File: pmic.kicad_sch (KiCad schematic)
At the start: 13 parts, among them J3 Battery Connector, SW2 PWR_BTN, U1 NPM1300-CAAA-R

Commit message: added peripherals pins
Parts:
- added C30, C31: 1u, symbol Device:C
- added C32, C33: 2.2u, symbol Device:C
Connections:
- net GND: now also C30.1, C31.1, C32.1, C33.1; no longer U1.B4 (LSIN1/VINLDO1), U1.B5 (LSIN2/VINLDO2)
- net VSYS: now also U1.B4 (LSIN1/VINLDO1), U1.B5 (LSIN2/VINLDO2), C30.2, C31.2
- net LSOUT1: now reaches U1.A4 (LSOUT1/VOUTLDO1)
- net LSOUT1: now also C33.2
- net LSOUT2: now reaches U1.A5 (LSOUT2/VOUTLDO2)
- net LSOUT2: now also C32.2
- no-connect marks 6 -> 4
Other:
- moved on the sheet: C22, D1

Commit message: assigned footprint and created PCB file
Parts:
- C20, C21: footprint (none) -> Capacitor_SMD:C_0805_2012Metric
- C22, C30, C31, C32, C33: footprint (none) -> Capacitor_SMD:C_0603_1608Metric
- D1: footprint (none) -> LED_SMD:LED_RGB_1210
- J3: footprint (none) -> Connector_PinHeader_2.54mm:PinHeader_1x02_P2.54mm_Vertical
- L1, L2: footprint (none) -> Inductor_SMD:L_0805_2012Metric
- R2, R3, R4, TH1: footprint (none) -> Resistor_SMD:R_0603_1608Metric
- SW2: footprint (none) -> Button_Switch_SMD:SW_Push_1P1T_NO_CK_KMR2
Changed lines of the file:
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@@
 			)
 		)
-		(property "Footprint" ""
+		(property "Footprint" "Capacitor_SMD:C_0603_1608Metric"
 			(at 116.5352 86.36 0)
 			(hide yes)
@@
 			)
 		)
-		(property "Footprint" ""
+		(property "Footprint" "Capacitor_SMD:C_0603_1608Metric"
 			(at 208.5848 86.36 0)
 			(hide yes)
@@
 			)
 		)
-		(property "Footprint" ""
+		(property "Footprint" "Button_Switch_SMD:SW_Push_1P1T_NO_CK_KMR2"
 			(at 204.47 124.46 0)
 			(hide yes)
@@
 			)
 		)
-		(property "Footprint" ""
+		(property "Footprint" "Resistor_SMD:R_0603_1608Metric"
 			(at 115.57 102.87 0)
 			(hide yes)
@@
 			)
 		)
-		(property "Footprint" ""
+		(property "Footprint" "Capacitor_SMD:C_0603_1608Metric"
 			(at 102.5652 86.36 0)
 			(hide yes)
@@
 			)
 		)
-		(property "Footprint" ""
+		(property "Footprint" "Resistor_SMD:R_0603_1608Metric"
 			(at 120.65 132.588 90)
 			(hide yes)
@@
 			)
 		)
-		(property "Footprint" ""
+		(property "Footprint" "Connector_PinHeader_2.54mm:PinHeader_1x02_P2.54mm_Vertical"
 			(at 71.12 57.15 0)
 			(hide yes)
@@
 			)
 		)
-		(property "Footprint" ""
+		(property "Footprint" "Inductor_SMD:L_0805_2012Metric"
 			(at 191.77 110.49 0)
 			(hide yes)
@@
 			)
 		)
-		(property "Footprint" ""
+		(property "Footprint" "Capacitor_SMD:C_0603_1608Metric"
 			(at 214.63 77.7748 0)
 			(hide yes)
@@
 			)
 		)
-		(property "Footprint" ""
+		(property "Footprint" "Resistor_SMD:R_0603_1608Metric"
 			(at 99.568 114.3 90)
 			(hide yes)
@@
 			)
 		)
-		(property "Footprint" ""
+		(property "Footprint" "LED_SMD:LED_RGB_1210"
 			(at 226.06 99.06 0)
 			(hide yes)
@@
 			)
 		)
-		(property "Footprint" ""
+		(property "Footprint" "Inductor_SMD:L_0805_2012Metric"
 			(at 193.04 120.65 0)
 			(hide yes)
@@
 			)
 		)
-		(property "Footprint" ""
+		(property "Footprint" "Capacitor_SMD:C_0603_1608Metric"
 			(at 197.1548 86.36 0)
 			(hide yes)
@@
 			)
 		)
-		(property "Footprint" ""
+		(property "Footprint" "Resistor_SMD:R_0603_1608Metric"
 			(at 110.998 115.57 90)
 			(hide yes)
@@
 			)
 		)
-		(property "Footprint" ""
+		(property "Footprint" "Capacitor_SMD:C_0805_2012Metric"
 			(at 180.34 57.4548 0)
 			(hide yes)
@@
 			)
 		)
-		(property "Footprint" ""
+		(property "Footprint" "Capacitor_SMD:C_0805_2012Metric"
 			(at 196.5452 74.93 0)
 			(hide yes)

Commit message: migrated display power with lora
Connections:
- net +3.3V_DISP renamed +3.3V_DP_LORA
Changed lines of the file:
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@@
 			)
 		)
-		(property "Value" "+3.3V_DISP"
+		(property "Value" "+3.3V_DP_LORA"
 			(at 201.93 109.2199 90)
 			(show_name no)

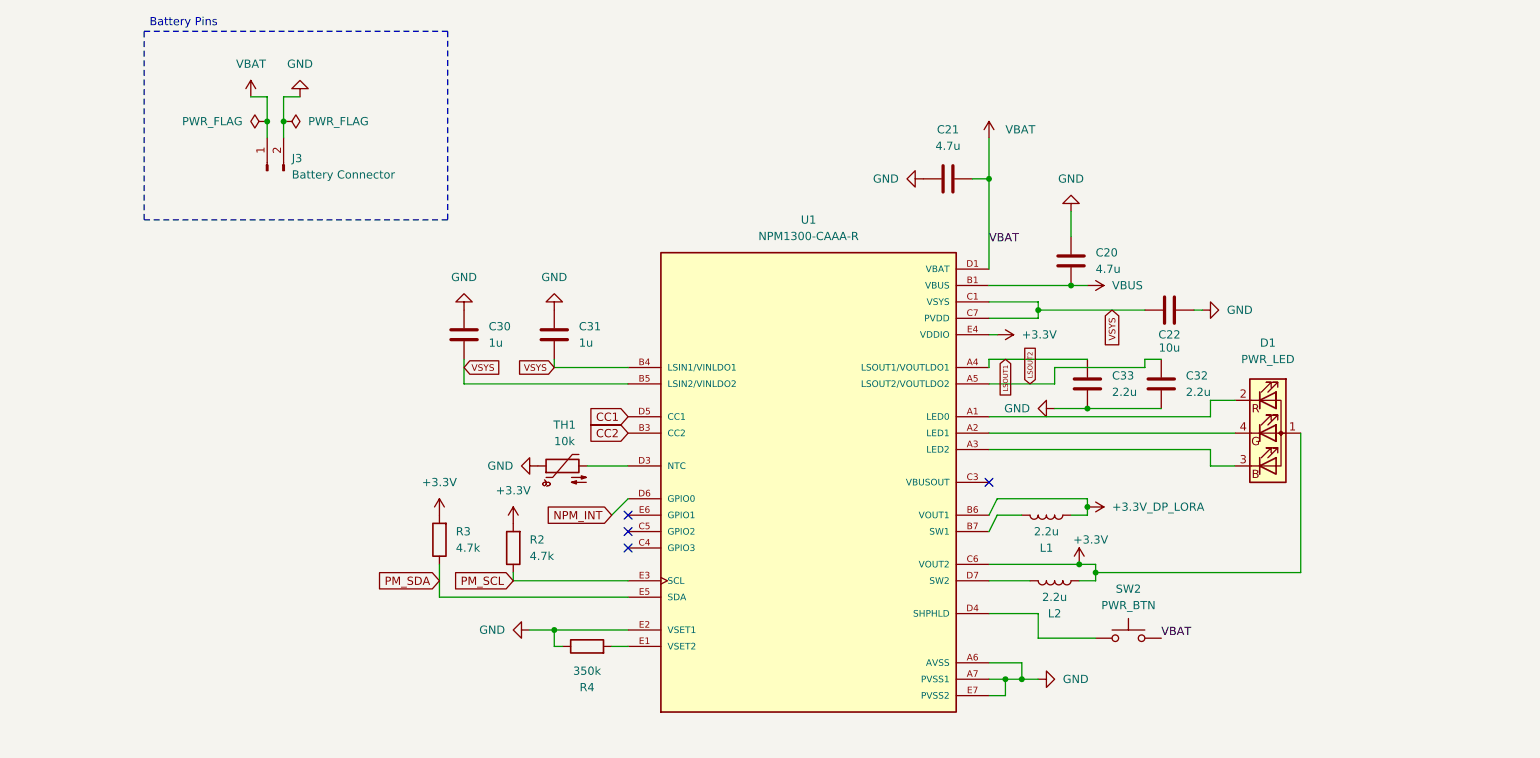
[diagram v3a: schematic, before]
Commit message: changed NPM1300 BGA to QFN package
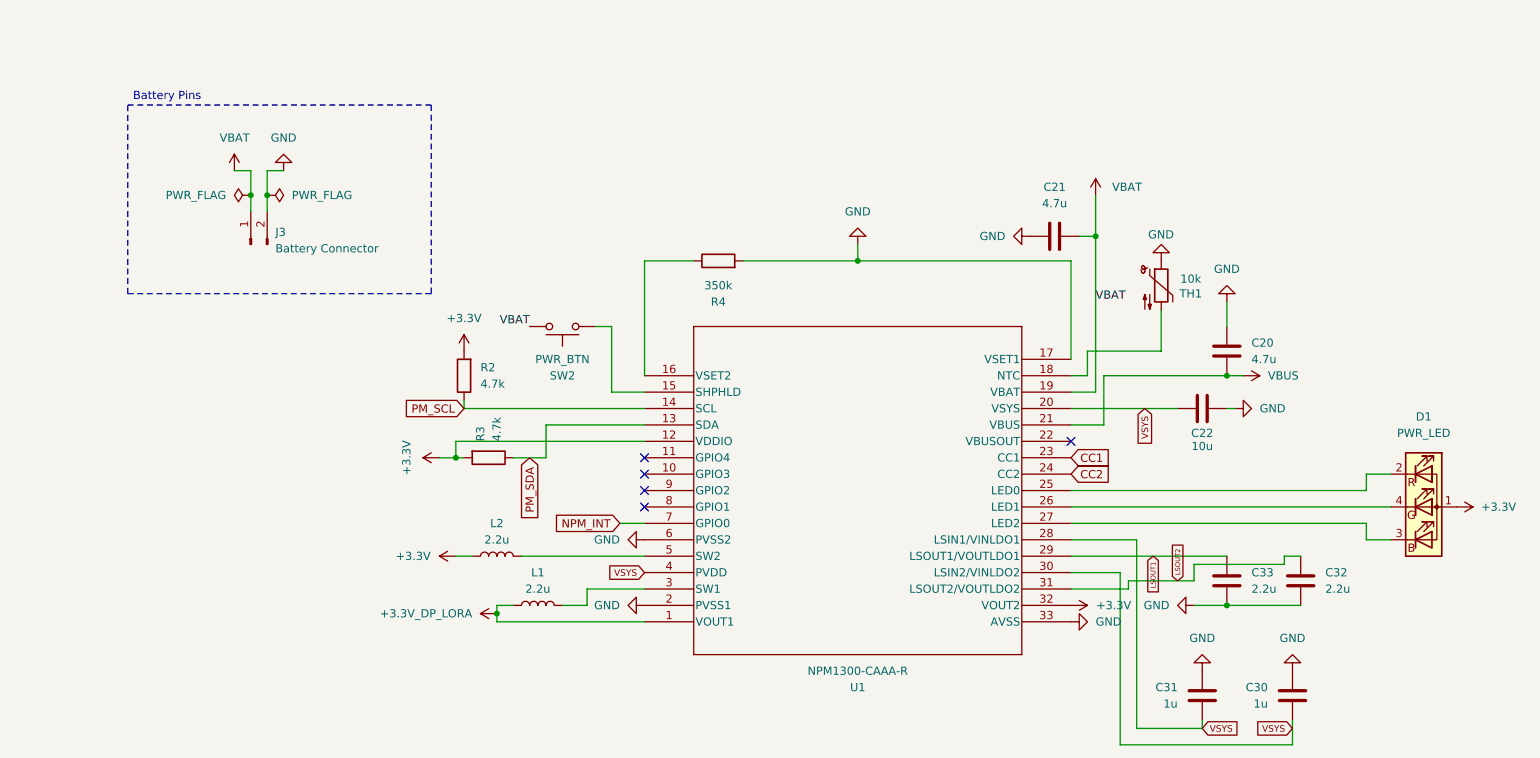
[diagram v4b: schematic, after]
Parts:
- U1: footprint TheSummitProject:BGA35N44X41P5X7_237X307X51 -> TheSummitProject:QFN32_5X5_NOR; symbol TheSummitProject:NPM1300-CAAA-R -> TheSummitProject:NPM1300-QEAA-R7
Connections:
- net +3.3V: now also U1.12 (VDDIO), U1.32 (VOUT2); no longer U1.C6 (VOUT2), U1.E4 (VDDIO)
- net +3.3V_DP_LORA: now also U1.1 (VOUT1); no longer U1.B6 (VOUT1)
- net CC1: now also U1.23 (CC1); no longer U1.D5 (CC1)
- net CC2: now also U1.24 (CC2); no longer U1.B3 (CC2)
- net GND: now also R4.2, U1.17 (VSET1), U1.2 (PVSS1), U1.33 (AVSS), U1.6 (PVSS2); no longer R4.1, U1.A6 (AVSS), U1.A7 (PVSS1), U1.E2 (VSET1), U1.E7 (PVSS2)
- net LSOUT1: now also U1.29 (LSOUT1/VOUTLDO1); no longer U1.A4 (LSOUT1/VOUTLDO1)
- net LSOUT2: now also U1.31 (LSOUT2/VOUTLDO2); no longer U1.A5 (LSOUT2/VOUTLDO2)
- net NPM_INT: now also U1.7 (GPIO0); no longer U1.D6 (GPIO0)
- net PM_SCL: now also U1.14 (SCL); no longer U1.E3 (SCL)
- net PM_SDA: now also U1.13 (SDA); no longer U1.E5 (SDA)
- net VBAT: now also U1.19 (VBAT); no longer U1.D1 (VBAT), U1.D2 (VBAT)
- net VBUS: now also U1.21 (VBUS); no longer U1.B1 (VBUS), U1.B2 (VBUS)
- net VSYS: now also U1.20 (VSYS), U1.28 (LSIN1/VINLDO1), U1.30 (LSIN2/VINLDO2), U1.4 (PVDD); no longer U1.B4 (LSIN1/VINLDO1), U1.B5 (LSIN2/VINLDO2), U1.C1 (VSYS), U1.C2 (VSYS), U1.C7 (PVDD)
- net at SW2.1: now also U1.15 (SHPHLD); no longer U1.D4 (SHPHLD)
- net at TH1.2: now also U1.18 (NTC); no longer U1.D3 (NTC)
- net at D1.2 (RK): now also U1.25 (LED0); no longer U1.A1 (LED0)
- net at D1.4 (GK): now also U1.26 (LED1); no longer U1.A2 (LED1)
- net at D1.3 (BK): now also U1.27 (LED2); no longer U1.A3 (LED2)
- net at L1.1: now also U1.3 (SW1); no longer U1.B7 (SW1)
- net at L2.1: now also U1.5 (SW2); no longer U1.D7 (SW2)
- new net: R4.1, U1.16 (VSET2)
- no-connect marks 4 -> 5
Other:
- moved on the sheet: C20, C21, C22, D1, J3, L1

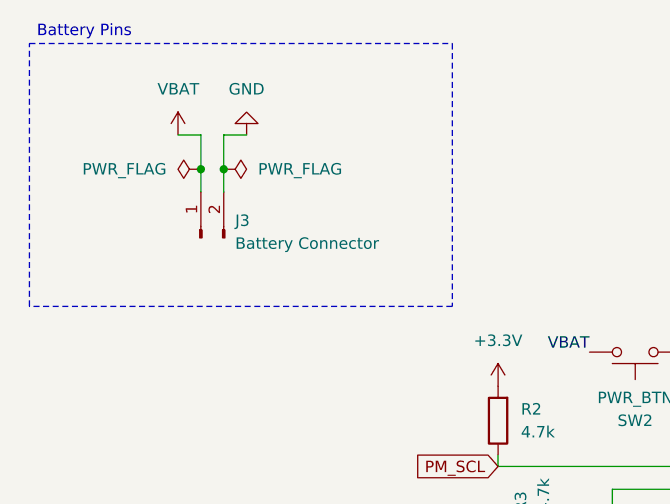
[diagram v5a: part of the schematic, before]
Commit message: Changed pcb to 4 layers and completed 50% traces
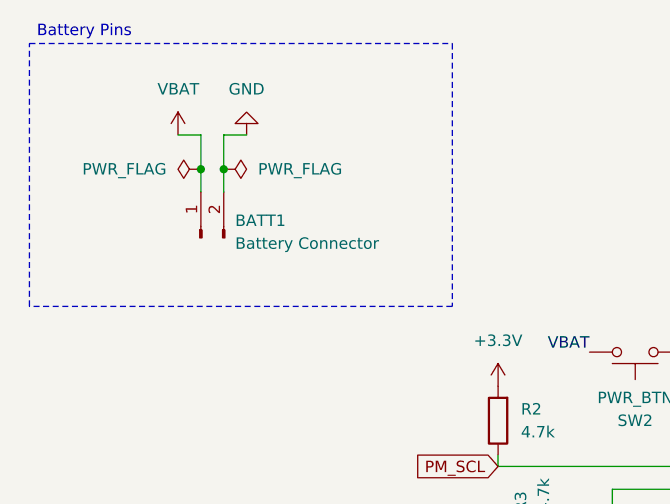
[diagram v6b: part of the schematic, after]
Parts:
- renumbered J3 to BATT1
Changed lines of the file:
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@@
 		(dnp no)
 		(fields_autoplaced yes)
-		(property "Reference" "J3"
+		(property "Reference" "BATT1"
 			(at 72.39 66.6749 90)
 			(show_name no)
@@
 			(project "TheSummitProject"
 				(path "/589d7319-43ab-496c-8236-77eb6db23a7f"
-					(reference "J3")
+					(reference "BATT1")
 					(unit 1)
 				)

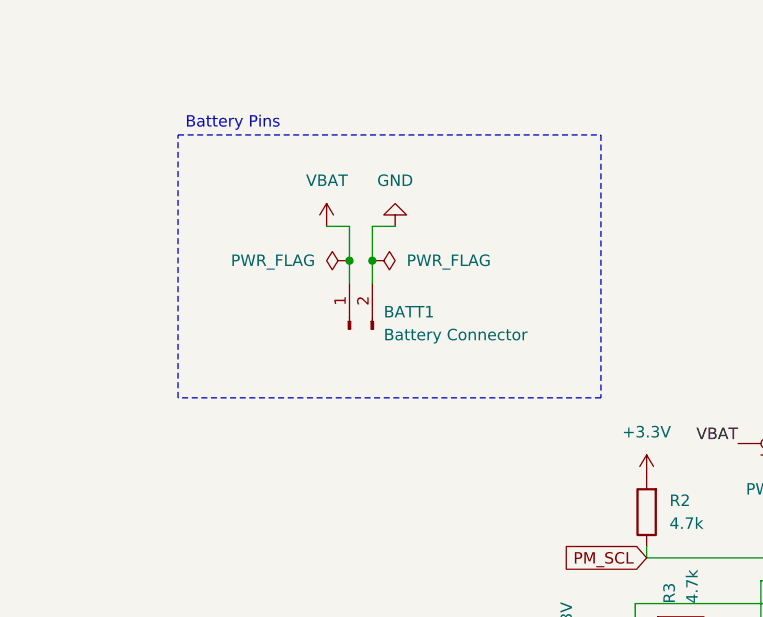
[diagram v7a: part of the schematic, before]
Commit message: Added reverse polarity protection circuit, PCB not implemented
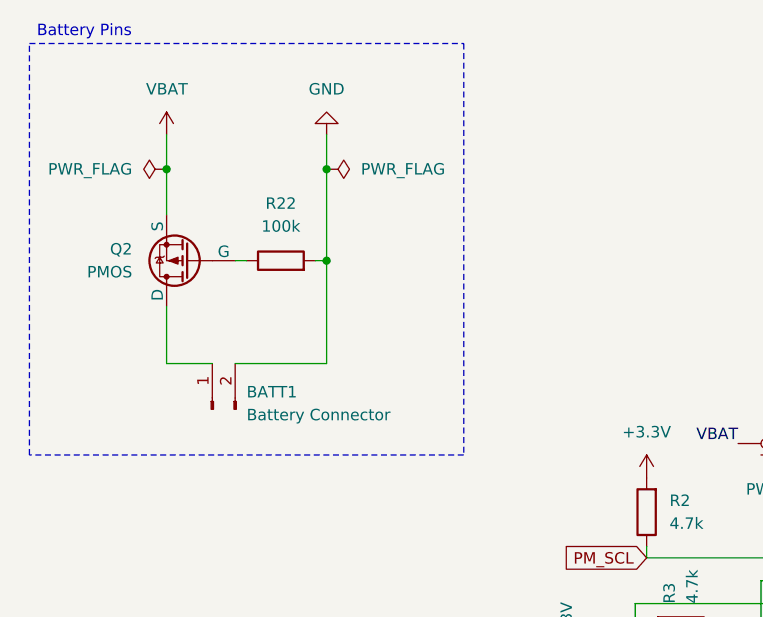
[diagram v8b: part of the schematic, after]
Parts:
- added Q2: PMOS, symbol Simulation_SPICE:PMOS
- added R22: 100k, symbol Device:R
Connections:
- net GND: now also R22.2
- net VBAT: now also Q2.3 (S); no longer BATT1.1 (Pin_1)
- new net: Q2.2 (G), R22.1
- new net: BATT1.1 (Pin_1), Q2.1 (D)
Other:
- moved on the sheet: BATT1
